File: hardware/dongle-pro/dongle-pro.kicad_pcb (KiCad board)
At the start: 4 copper layers, 26 x 98 mm, 111 parts, among them J1 TYPE-C24PQT, J2 TYPE-C24PQT, J3 TC2030-IDC-NL, SW1 TS-1187A-B-A-B, U1 RP2354A, U10 AP22653W6-7, U2 FUSB302BMPX, U3 HD3SS3220RNHR, U4 GL3510-OSY52, U5 RT9013-33GB, U6 TLV70212DBVR, U7 HD3SS3212IRKSR, U8 74AVC1T45GW,125, U9 74AVC1T45GW,125, Y1 X322512MSB4SI, Y2 25MHz

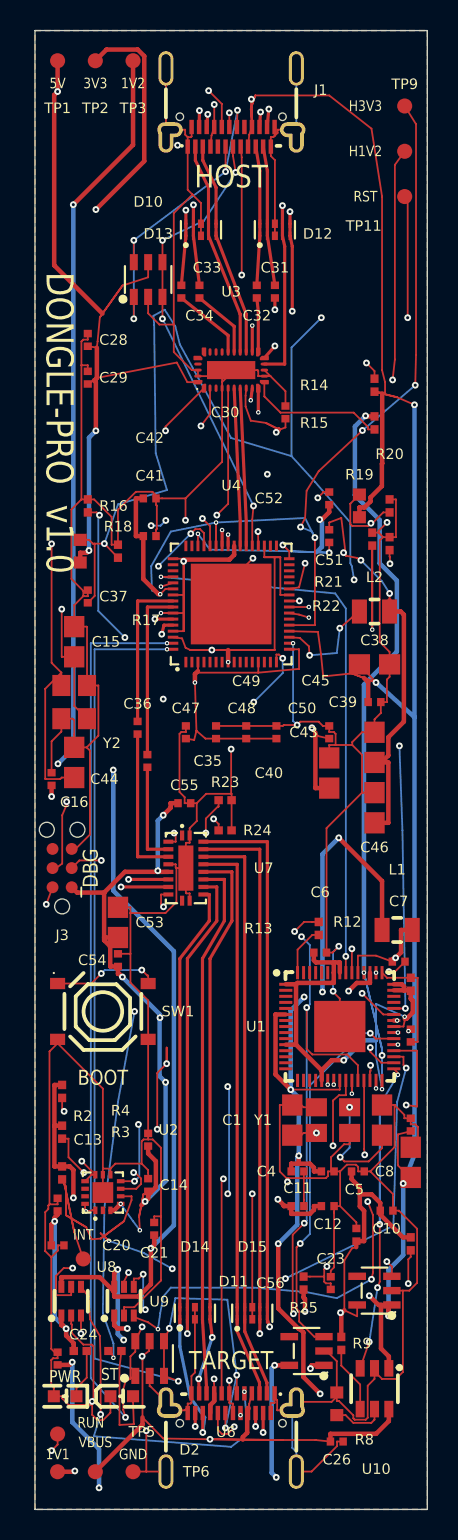
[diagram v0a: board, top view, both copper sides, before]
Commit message: Length-tune the Dongle-Pro SuperSpeed pairs
New gen/tune.py pipeline step measures each SS pair's intra-pair length
mismatch on the routed board and nulls it with 45-degree serpentine
bumps on the shorter member, sized from the live measurement so the
step stays correct across reruns. The five pairs that were 1-2mm off
(HUB_DRX/DTX, TGT_TX1/TX2/RX2, up to ~13ps) are now all under 0.2mm
(~1.3ps); the short mux-to-hub links stay within ~5ps and are left
alone. Also fix two latent regen bugs the rerun exposed (board.py exec
lost __file__ after the rename; recreating zones after removal
segfaults pcbnew, so the pours are now reused and refilled in place)
and refresh the fab package. DRC stays at 0 errors, 0 unconnected.
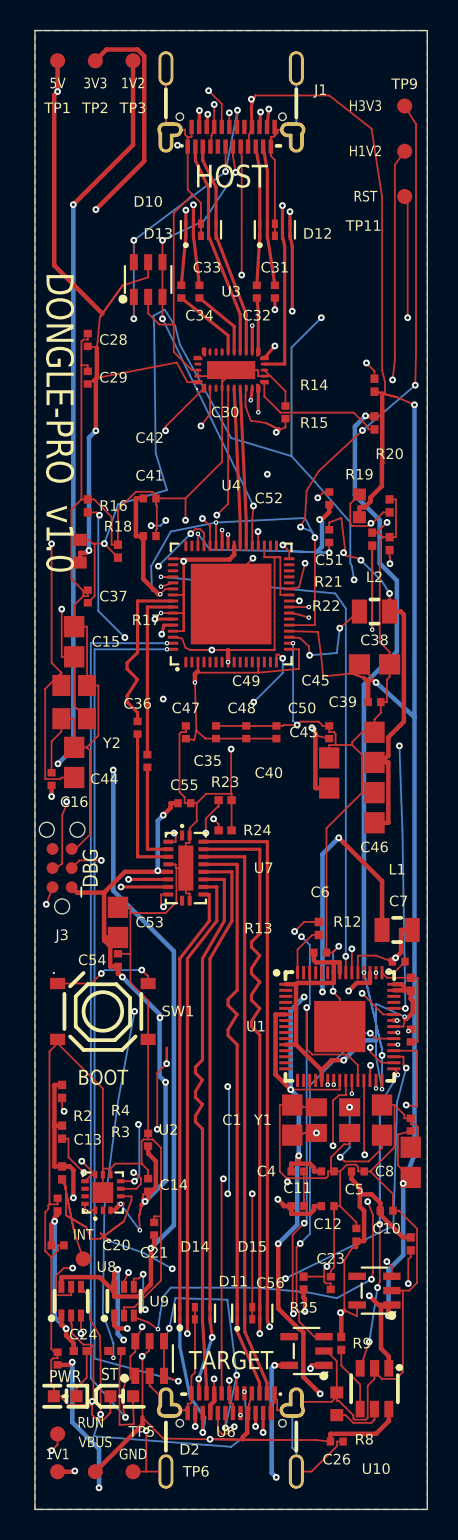
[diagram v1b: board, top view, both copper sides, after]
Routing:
- net HUB_DRX_P: track 20.9 -> 22.8 mm
- net TGT_TX2_N: track 42.9 -> 44.5 mm
- net HUB_DTX_N: track 10.3 -> 11.4 mm
- net TGT_TX1_N: track 35.8 -> 36.9 mm
- net TGT_RX2_N: track 37.6 -> 38.5 mm
